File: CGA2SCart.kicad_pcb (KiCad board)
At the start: 2 copper layers, 67 x 66 mm, 34 parts, among them J1 SCART-F, J2 DB9_Male, J3 Audio-Jack-3_2Switches, J4 DB15_Female_HighDensity, Q1 2N7000

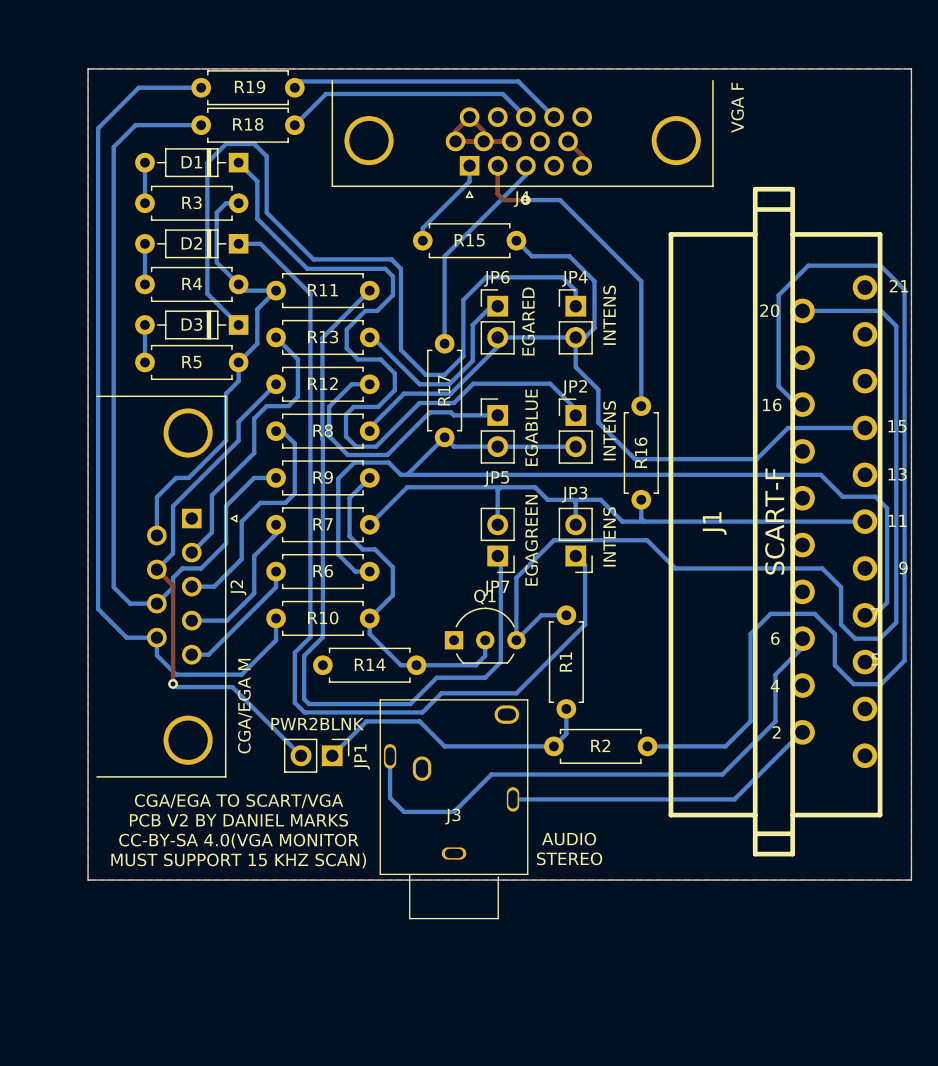
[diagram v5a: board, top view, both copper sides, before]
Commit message: V3 of CGA2SCART, change CSYNC to XOR presync
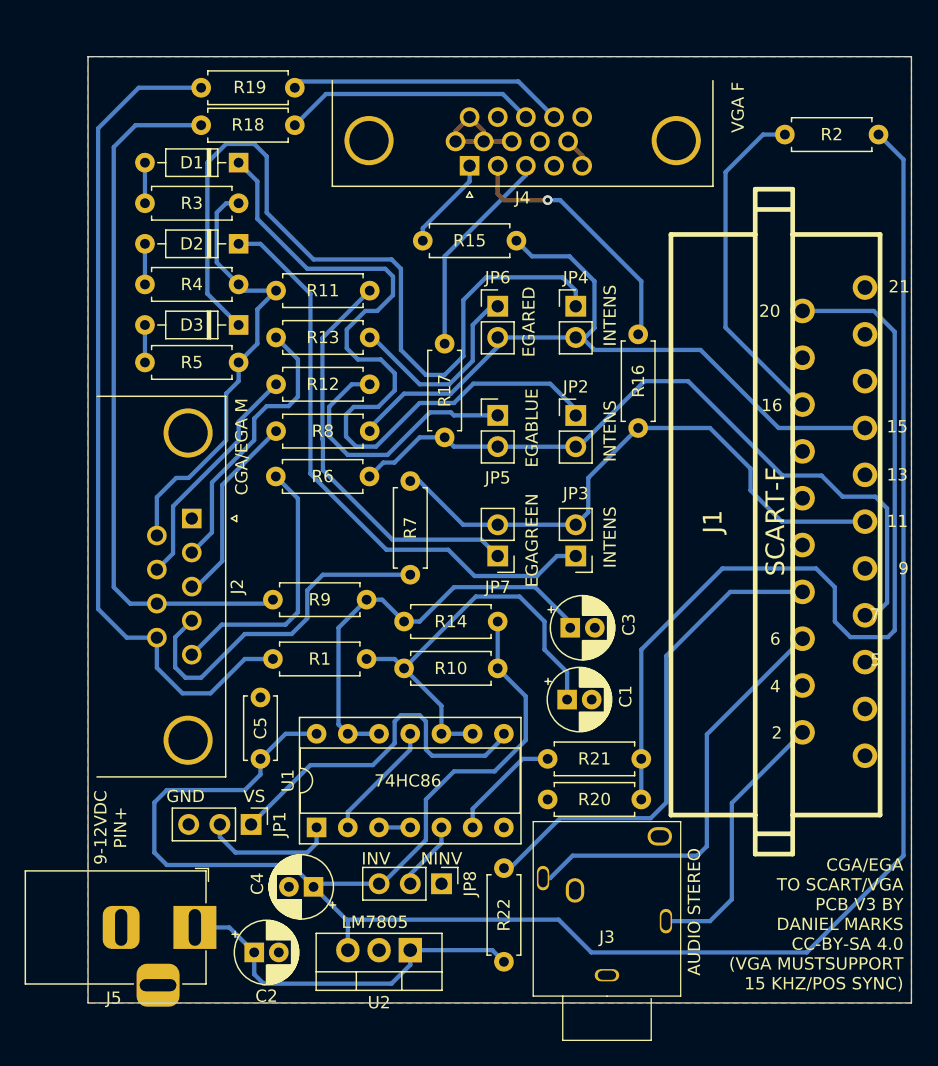
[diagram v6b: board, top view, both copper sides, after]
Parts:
- removed Q1: 2N7000, Package_TO_SOT_THT:TO-92_Inline_Wide
- added C1: 10 uF, Capacitor_THT:CP_Radial_D5.0mm_P2.00mm, F.Cu at (138.0, 99.3)
- added C2: 10 uF, Capacitor_THT:CP_Radial_D5.0mm_P2.00mm, F.Cu at (112.5, 119.9)
- added C3: 10 uF, Capacitor_THT:CP_Radial_D5.0mm_P2.00mm, F.Cu at (138.2, 93.5)
- added C4: 10 uF, Capacitor_THT:CP_Radial_D5.0mm_P2.00mm, F.Cu at (117.3, 114.6)
- added C5: 100 nF, Capacitor_THT:C_Disc_D5.0mm_W2.5mm_P5.00mm, F.Cu at (113.0, 104.1)
- added J5: Barrel_Jack_Switch, Connector_BarrelJack:BarrelJack_Horizontal, F.Cu at (107.7, 117.9)
- added JP8: POLARITY, Connector_PinHeader_2.54mm:PinHeader_1x03_P2.54mm_Vertical, F.Cu at (127.8, 114.3)
- added R20: 220R, Resistor_THT:R_Axial_DIN0207_L6.3mm_D2.5mm_P7.62mm_Horizontal, F.Cu at (136.4, 107.4)
- added R21: 220R, Resistor_THT:R_Axial_DIN0207_L6.3mm_D2.5mm_P7.62mm_Horizontal, F.Cu at (144.0, 104.1)
- added R22: 1k5, Resistor_THT:R_Axial_DIN0207_L6.3mm_D2.5mm_P7.62mm_Horizontal, F.Cu at (132.8, 113.0)
- added U1: 74HC86, Package_DIP:DIP-14_W7.62mm_Socket, F.Cu at (117.6, 109.7)
- added U2: LM7805_TO220, Package_TO_SOT_THT:TO-220-3_Vertical, F.Cu at (125.2, 119.7)
- JP1: value PWR2BLNK -> HSYNC/CSYNC; footprint Connector_PinHeader_2.54mm:PinHeader_1x02_P2.54mm_Vertical -> Connector_PinHeader_2.54mm:PinHeader_1x03_P2.54mm_Vertical
- R1, R9: value 470R -> 1k
- R10: value 470R -> 2k2
- R14: value 1M -> 2k2
- moved R2 51.0 mm to (155.7, 53.3), turned to 0 degrees
- moved R1 24.2 mm to (114.0, 96.0), turned to 0 degrees
- moved R10 18.5 mm to (132.3, 96.8), turned to 180 degrees
- moved J3 15.9 mm to (141.2, 123.4)
- moved R7 11.7 mm to (125.2, 89.2), turned to 90 degrees
- moved R9 9.91 mm to (114.0, 91.2)
- moved JP1 8.65 mm to (112.3, 109.5)
- moved R6 7.74 mm to (114.3, 81.2)
- moved R14 7.50 mm to (132.3, 93.0)
- moved R16 5.85 mm to (143.8, 69.6)
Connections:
- J1 pad 18: unconnected-(J1-Pad18) -> GND
- J1 pad 8: unconnected-(J1-Pad8) -> Net-(J1-Pad8)
- JP1 pad 2: EGA_BLUE -> Net-(JP1-Pad2)
- R1 pad 1: Net-(JP1-Pad1) -> CGA_VSYNC
- R1 pad 2: Net-(J1-Pad20) -> Net-(C1-Pad1)
- R10 pad 1: CGA_VSYNC -> +5V
- R10 pad 2: Net-(Q1-Pad2) -> Net-(C1-Pad1)
- R14 pad 1: Net-(Q1-Pad2) -> +5V
- R14 pad 2: GND -> Net-(C3-Pad1)
- R2 pad 2: Net-(JP1-Pad1) -> +5V
- R9 pad 2: Net-(Q1-Pad2) -> Net-(C3-Pad1)
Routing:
- net +5V: track 0.00 -> 184.7 mm
- net Net-(J1-Pad16): track 85.8 -> 27.6 mm
- net Net-(J1-Pad8): track 0.00 -> 40.6 mm
- net Net-(C3-Pad1): track 0.00 -> 34.8 mm
- net Net-(C1-Pad1): track 0.00 -> 34.3 mm
- net +12V: track 0.00 -> 30.3 mm
- net Net-(JP7-Pad1): track 61.8 -> 33.3 mm
- net Net-(Q1-Pad2): track 28.2 -> 0.00 mm
- net Net-(D2-Pad1): track 74.1 -> 47.9 mm
- net EGA_BLUE: track 41.8 -> 19.1 mm, vias 1 -> 0
- net Net-(J1-Pad7): track 80.5 -> 59.4 mm
- net CGA_GREEN: track 12.3 -> 28.7 mm
- net CGA_BLUE: track 10.4 -> 21.9 mm
- net Net-(J1-Pad6): track 45.9 -> 34.5 mm
- net Net-(JP1-Pad2): track 0.00 -> 11.0 mm
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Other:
- board size 67 x 66 mm -> 67 x 77 mm
- board text added: "74HC86"
- board text added: "9-12VDC PIN+"
- board text added: "CGA/EGA TO SCART/VGA PCB V3 BY DANIEL MARKS CC-BY-SA 4.0 (VGA MUSTSUPPORT 15 KHZ/POS SYNC)"
- board text added: "GND"
- board text added: "INV"
- board text added: "LM7805"
- board text added: "NINV"
- board text added: "VS"
- board text removed: "CGA/EGA TO SCART/VGA PCB V2 BY DANIEL MARKS CC-BY-SA 4.0(VGA MONITOR MUST SUPPORT 15 KHZ SCAN)"
- board text removed: "PWR2BLNK"

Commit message: Fixed stupid double XOR thing, why can't I get this right?
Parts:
- removed R10, R14: 2k2, Resistor_THT:R_Axial_DIN0207_L6.3mm_D2.5mm_P7.62mm_Horizontal
- C1, C3: value 10 uF -> 1 uF
- R1, R9: value 1k -> 10k
- moved C3 13.0 mm to (125.2, 94.0)
- moved R7 11.7 mm to (114.3, 84.8), turned to 0 degrees
- moved C1 5.24 mm to (132.8, 98.3), turned to 90 degrees
- moved R9 1.27 mm to (114.0, 92.5)
- moved J5 0.76 mm to (107.7, 117.1)
- moved R1 0.25 mm to (113.8, 96.0)
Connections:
- U1 pad 10: Net-(C1-Pad1) -> CGA_VSYNC
- U1 pad 13: Net-(C3-Pad1) -> CGA_HSYNC
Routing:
- net +5V: track 184.7 -> 154.5 mm
- net CGA_VSYNC: track 68.5 -> 90.5 mm
- net CGA_HSYNC: track 57.3 -> 76.3 mm
- net Net-(C1-Pad1): track 34.3 -> 16.3 mm
- net Net-(C3-Pad1): track 34.8 -> 16.9 mm
- net CGA_GREEN: track 28.7 -> 11.8 mm
- net Net-(J1-Pad11): track 47.6 -> 60.5 mm
- net CGA_BLUE: track 21.9 -> 19.0 mm
- net Net-(D2-Pad1): track 47.9 -> 50.2 mm
- net Net-(JP1-Pad2): track 11.0 -> 9.84 mm
- net Net-(JP1-Pad1): track 28.9 -> 29.4 mm
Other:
- board text added: "9-12 VDC PIN+"
- board text added: "CGA/EGA TO SCART/VGA PCB V3 BY DANIEL MARKS CC-BY-SA 4.0 (VGA MUST SUPPORT 15 KHZ/POS SYNC)"
- board text removed: "9-12VDC PIN+"
- board text removed: "CGA/EGA TO SCART/VGA PCB V3 BY DANIEL MARKS CC-BY-SA 4.0 (VGA MUSTSUPPORT 15 KHZ/POS SYNC)"

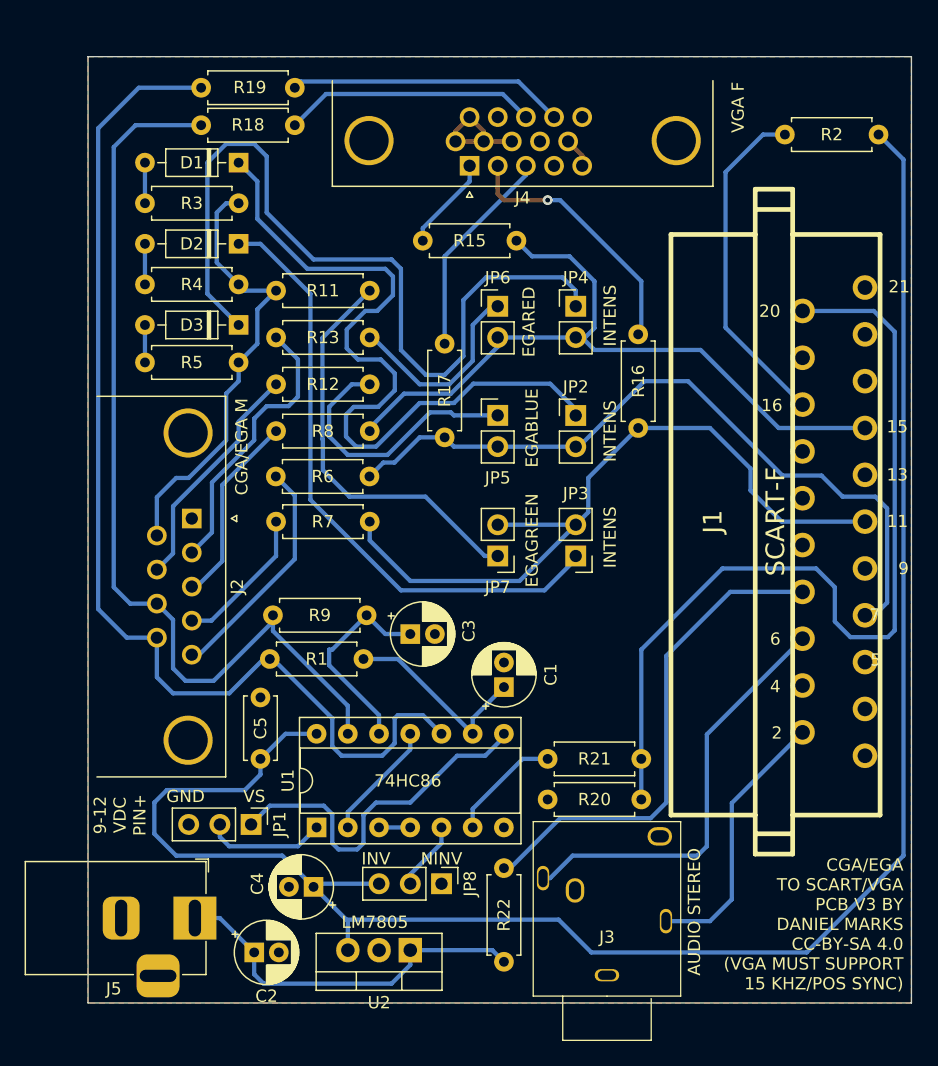
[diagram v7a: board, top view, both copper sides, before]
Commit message: Added CSYNC to VGA option
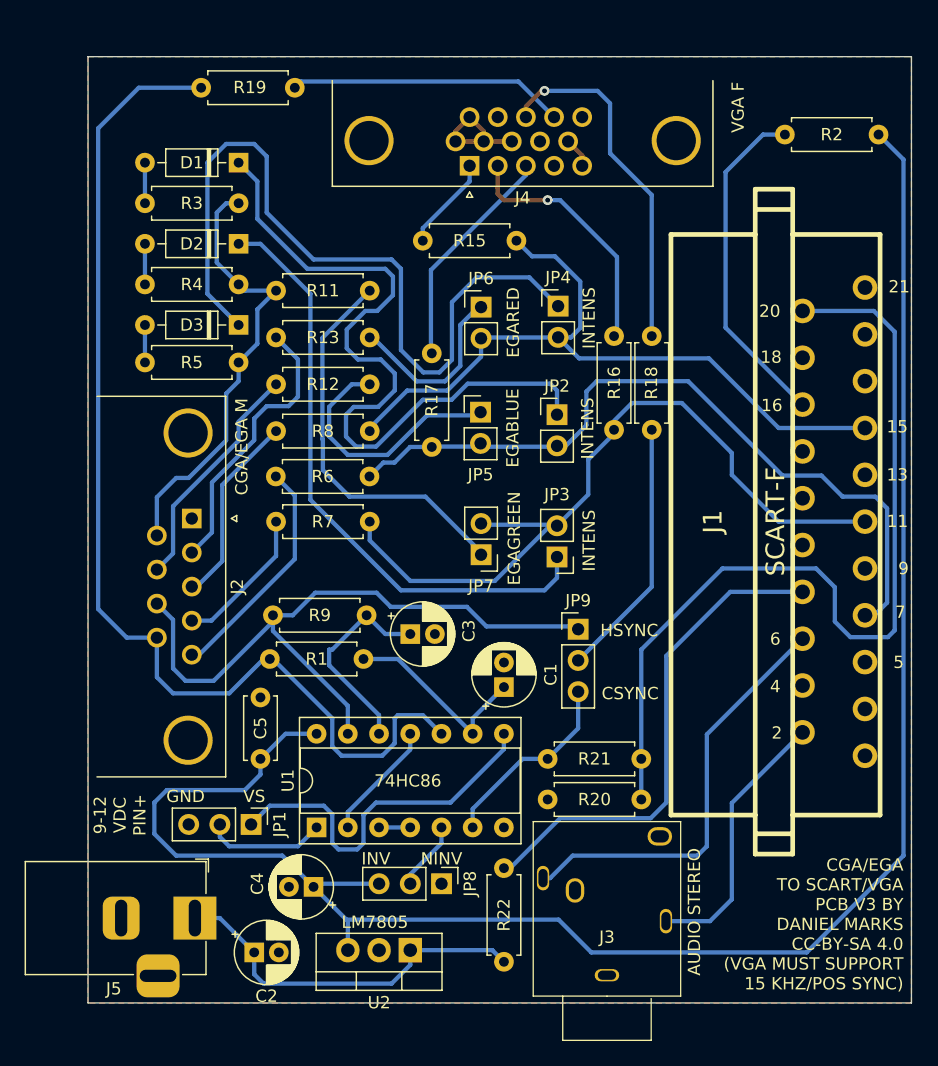
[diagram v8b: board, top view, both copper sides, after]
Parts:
- added JP9: COMPS, Connector_PinHeader_2.54mm:PinHeader_1x03_P2.54mm_Vertical, F.Cu at (138.9, 93.6)
- moved R18 44.3 mm to (144.9, 77.4), turned to 90 degrees
- moved R16 1.97 mm to (141.8, 69.7)
- moved JP3 1.53 mm to (137.2, 87.7)
- moved JP2 1.53 mm to (137.2, 76.1)
- moved JP4 1.43 mm to (137.2, 67.3)
- moved JP5 1.42 mm to (130.9, 75.9)
- moved JP7 1.36 mm to (131.0, 87.5)
- moved JP6 1.36 mm to (131.0, 67.4)
- moved R17 1.31 mm to (127.0, 71.1)
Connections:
- R18 pad 1: CGA_HSYNC -> Net-(R18-Pad1)
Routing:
- net Net-(R18-Pad1): track 0.00 -> 21.3 mm
- net CGA_HSYNC: track 76.3 -> 55.3 mm
- net VGA_HSYNC: track 20.6 -> 28.1 mm, vias 0 -> 1
- net Net-(R21-Pad2): track 9.30 -> 15.8 mm
- net Net-(D3-Pad1): track 66.9 -> 64.6 mm
- net Net-(JP5-Pad1): track 22.3 -> 20.8 mm
- net Net-(JP6-Pad1): track 16.3 -> 15.0 mm
- net Net-(JP7-Pad1): track 33.3 -> 32.1 mm
- net VGA_BLUE: track 17.2 -> 18.5 mm
- net Net-(J1-Pad7): track 59.4 -> 60.6 mm
- net Net-(D2-Pad1): track 50.2 -> 49.5 mm
- net Net-(D1-Pad1): track 61.4 -> 60.7 mm
- net VGA_GREEN: track 21.3 -> 20.7 mm
- net Net-(JP1-Pad1): track 29.4 -> 30.0 mm
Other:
- board text added: "18"
- board text added: "CSYNC"
- board text added: "HSYNC"
